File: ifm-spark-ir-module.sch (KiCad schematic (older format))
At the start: 0 parts

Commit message: Created symbol for TSOP75338TT and added to schematic
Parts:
- added IR?: TSOP75338TT, symbol TSOP75338TT
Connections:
- new net GND: IR?.1 (GND), IR?.4 (GND)
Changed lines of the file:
@@
 EESchema Schematic File Version 2
+LIBS:ic-digital
 LIBS:power
 LIBS:device
@@
 LIBS:contrib
 LIBS:valves
+LIBS:ifm-spark-ir-module-cache
 EELAYER 25 0
 EELAYER END
@@
 Comment4 ""
 $EndDescr
+$Comp
+L TSOP75338TT IR?
+U 1 1 59279B4C
+P 5450 3850
+F 0 "IR?" H 5550 4350 60  0000 C CNN
+F 1 "TSOP75338TT" H 5450 4000 60  0000 C CNN
+F 2 "" H 5450 3850 60  0001 C CNN
+F 3 "http://www.vishay.com/docs/82495/tsop753.pdf" H 5450 3850 60  0001 C CNN
+F 4 "TSOP75338TT" H 5450 3850 60  0001 C CNN "MPN"
+F 5 "TSOP75338TTCT-ND" H 5450 3850 60  0001 C CNN "DKPN"
+	1    5450 3850
+	1    0    0    -1
+$EndComp
 $EndSCHEMATC

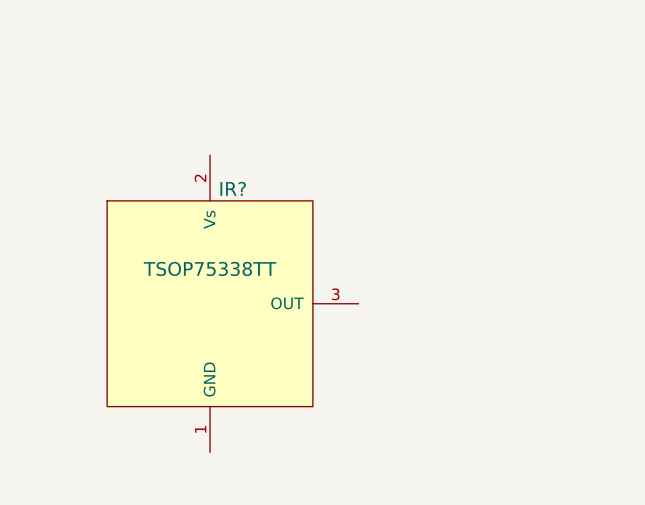
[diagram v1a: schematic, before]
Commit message: Added in passives and connector and wired it up
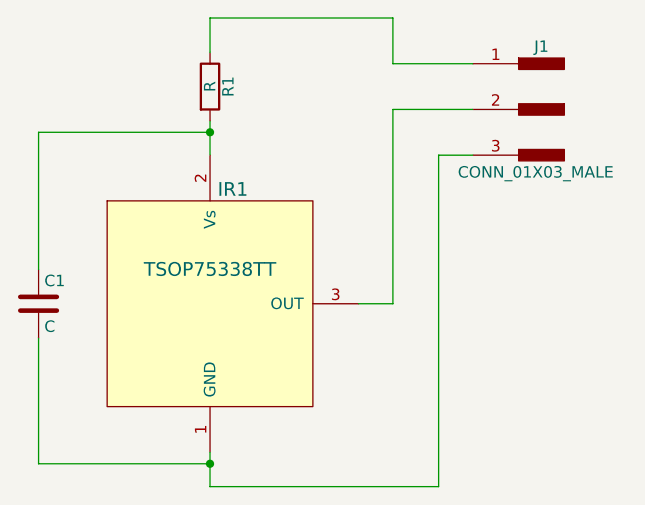
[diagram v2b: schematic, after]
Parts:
- added C1: C, Capacitors_SMD:C_0805_HandSoldering, symbol C
- added J1: CONN_01X03_MALE, Pin_Headers:Pin_Header_Straight_1x03_Pitch2.54mm, symbol CONN_01X03_MALE
- added R1: R, Resistors_SMD:R_0805_HandSoldering, symbol R
- IR1: renamed from IR?; footprint (none) -> ifm-ic-digital:TSOP75x
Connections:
- net GND: now also C1.2, J1.3
- net at IR1.2 (Vs): now also C1.1, R1.2
- net at IR1.3 (OUT): now also J1.2
- new net: J1.1, R1.1
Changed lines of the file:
@@
 $EndDescr
 $Comp
-L TSOP75338TT IR?
+L TSOP75338TT IR1
 U 1 1 59279B4C
 P 5450 3850
-F 0 "IR?" H 5550 4350 60  0000 C CNN
+F 0 "IR1" H 5550 4350 60  0000 C CNN
 F 1 "TSOP75338TT" H 5450 4000 60  0000 C CNN
-F 2 "" H 5450 3850 60  0001 C CNN
+F 2 "ifm-ic-digital:TSOP75x" H 5450 3850 60  0001 C CNN
 F 3 "http://www.vishay.com/docs/82495/tsop753.pdf" H 5450 3850 60  0001 C CNN
 F 4 "TSOP75338TT" H 5450 3850 60  0001 C CNN "MPN"
@@
 	1    0    0    -1
 $EndComp
+$Comp
+L C C1
+U 1 1 59279C91
+P 4700 3850
+F 0 "C1" H 4725 3950 50  0000 L CNN
+F 1 "C" H 4725 3750 50  0000 L CNN
+F 2 "Capacitors_SMD:C_0805_HandSoldering" H 4738 3700 50  0001 C CNN
+F 3 "" H 4700 3850 50  0001 C CNN
+	1    4700 3850
+	1    0    0    -1
+$EndComp
+$Comp
+L R R1
+U 1 1 59279D4A
+P 5450 2900
+F 0 "R1" V 5530 2900 50  0000 C CNN
+F 1 "R" V 5450 2900 50  0000 C CNN
+F 2 "Resistors_SMD:R_0805_HandSoldering" V 5380 2900 50  0001 C CNN
+F 3 "" H 5450 2900 50  0001 C CNN
+	1    5450 2900
+	1    0    0    -1
+$EndComp
+$Comp
+L CONN_01X03_MALE J1
+U 1 1 59279E57
+P 6900 3000
+F 0 "J1" H 6900 3275 50  0000 C CNN
+F 1 "CONN_01X03_MALE" H 6925 2725 50  0000 C CNN
+F 2 "Pin_Headers:Pin_Header_Straight_1x03_Pitch2.54mm" H 6900 3200 50  0001 C CNN
+F 3 "" H 6900 3200 50  0001 C CNN
+	1    6900 3000
+	-1   0    0    -1
+$EndComp
+Wire Wire Line
+	5450 3200 5450 3050
+Wire Wire Line
+	4700 3700 4700 3100
+Wire Wire Line
+	4700 3100 5450 3100
+Connection ~ 5450 3100
+Wire Wire Line
+	5450 4500 5450 4650
+Wire Wire Line
+	5450 4650 6450 4650
+Wire Wire Line
+	6450 4650 6450 3200
+Wire Wire Line
+	6450 3200 6600 3200
+Wire Wire Line
+	6100 3850 6250 3850
+Wire Wire Line
+	6250 3850 6250 3000
+Wire Wire Line
+	6250 3000 6600 3000
+Wire Wire Line
+	5450 2750 5450 2600
+Wire Wire Line
+	5450 2600 6250 2600
+Wire Wire Line
+	6250 2600 6250 2800
+Wire Wire Line
+	6250 2800 6600 2800
+Wire Wire Line
+	4700 4000 4700 4550
+Wire Wire Line
+	4700 4550 5450 4550
+Connection ~ 5450 4550
 $EndSCHEMATC
